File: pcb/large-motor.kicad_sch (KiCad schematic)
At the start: 3 parts, among them U13 ACS780xLRTR-100B

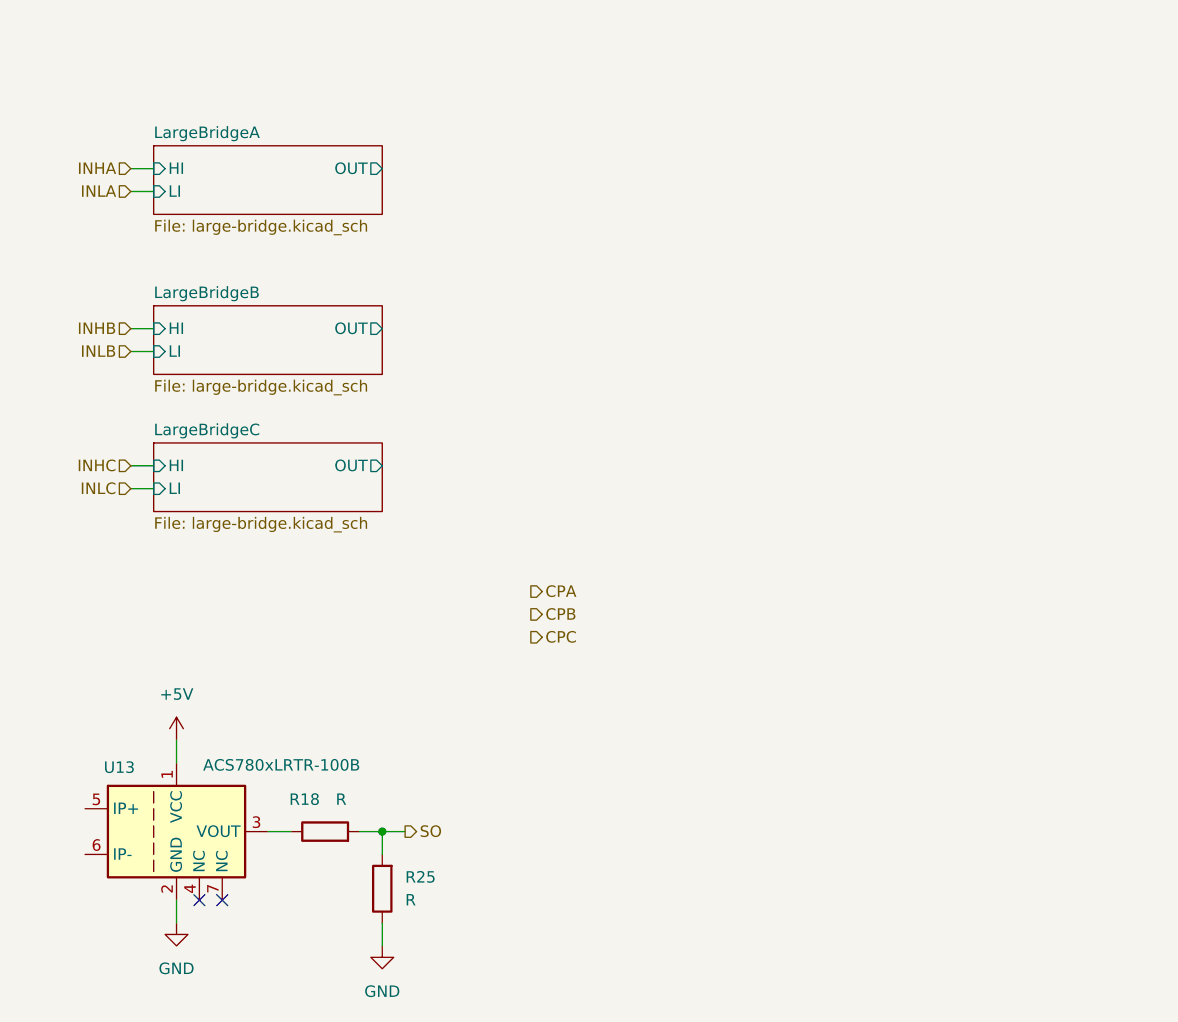
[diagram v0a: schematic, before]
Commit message: Finish rough layout
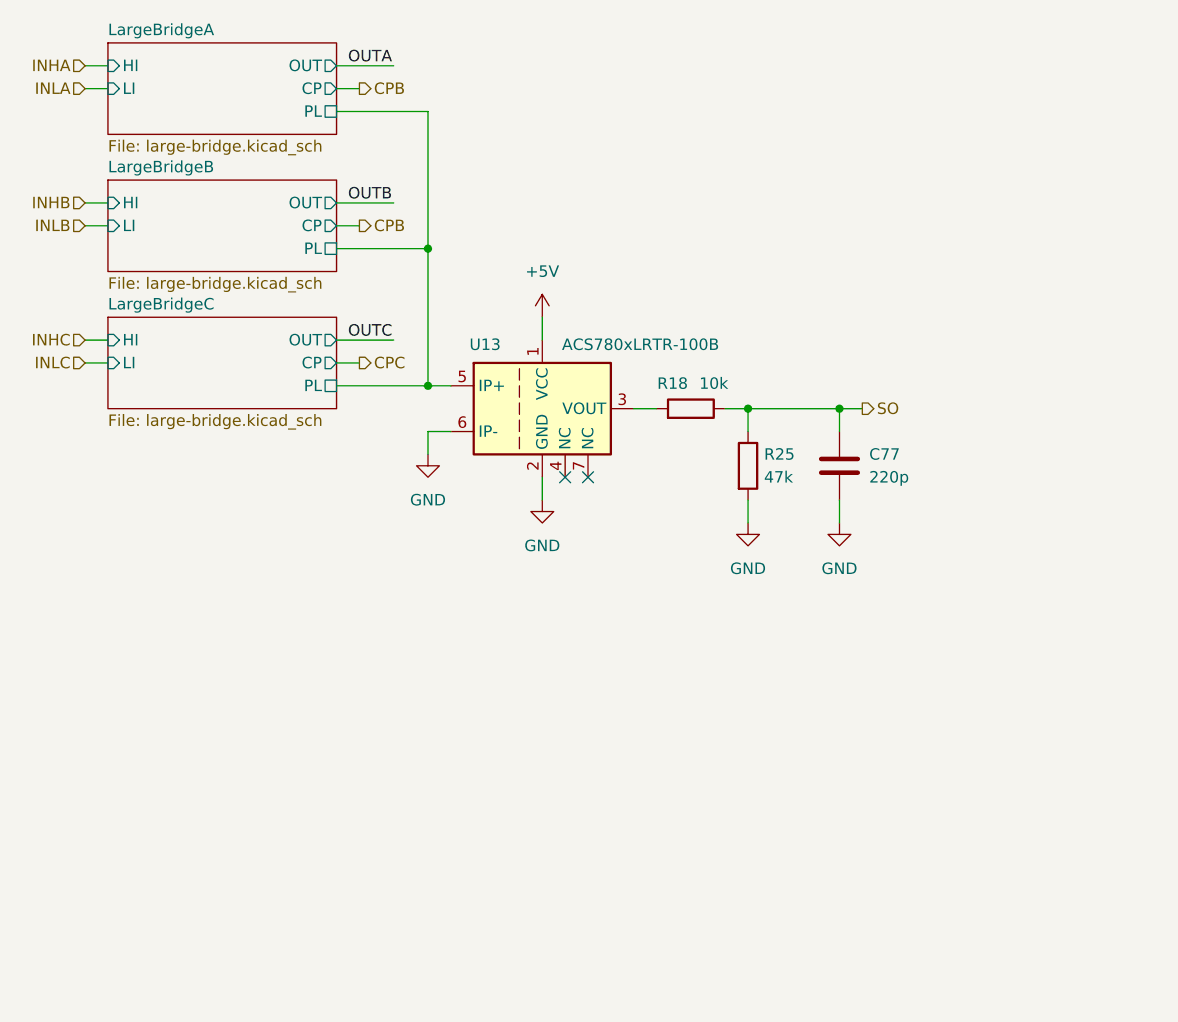
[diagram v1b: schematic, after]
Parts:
- added C77: 220p, Resistor_SMD:R_0402_1005Metric, symbol Device:C
- R18: value R -> 10k; LCSC (none) -> C25744
- R25: value R -> 47k; LCSC (none) -> C25792
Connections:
- net GND: now also R25.2, U13.6 (IP-), C77.2; no longer R25.1
- net SO: now also R18.1, R25.1, C77.1; no longer R18.2, R25.2
- net at U13.3 (VOUT): now also R18.2; no longer R18.1
- net LargeBridgeA/PL: now reaches U13.5 (IP+)
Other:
- sheet LargeBridgeA ports: added CP, PL; removed none
- sheet LargeBridgeB ports: added CP, PL; removed none
- sheet LargeBridgeC ports: added CP, PL; removed none
- moved on the sheet: U13

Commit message: Save old buck regulator
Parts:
- added C70: 22u, Capacitor_SMD:C_0805_2012Metric, symbol Device:C
- added C71: 100n, Capacitor_SMD:C_0402_1005Metric, symbol Device:C
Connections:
- net +5V: now also C71.1
- net GND: now also C70.2, C71.2
- new net VDD: C70.1

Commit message: Finish pcb
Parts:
- added C1, C2, C3: 22u, Capacitor_SMD:C_0805_2012Metric, symbol Device:C
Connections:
- net GND: now also C1.2, C2.2, C3.2
- net VDD: now also C1.1, C2.1, C3.1
